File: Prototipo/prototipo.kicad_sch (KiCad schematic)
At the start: 13 parts

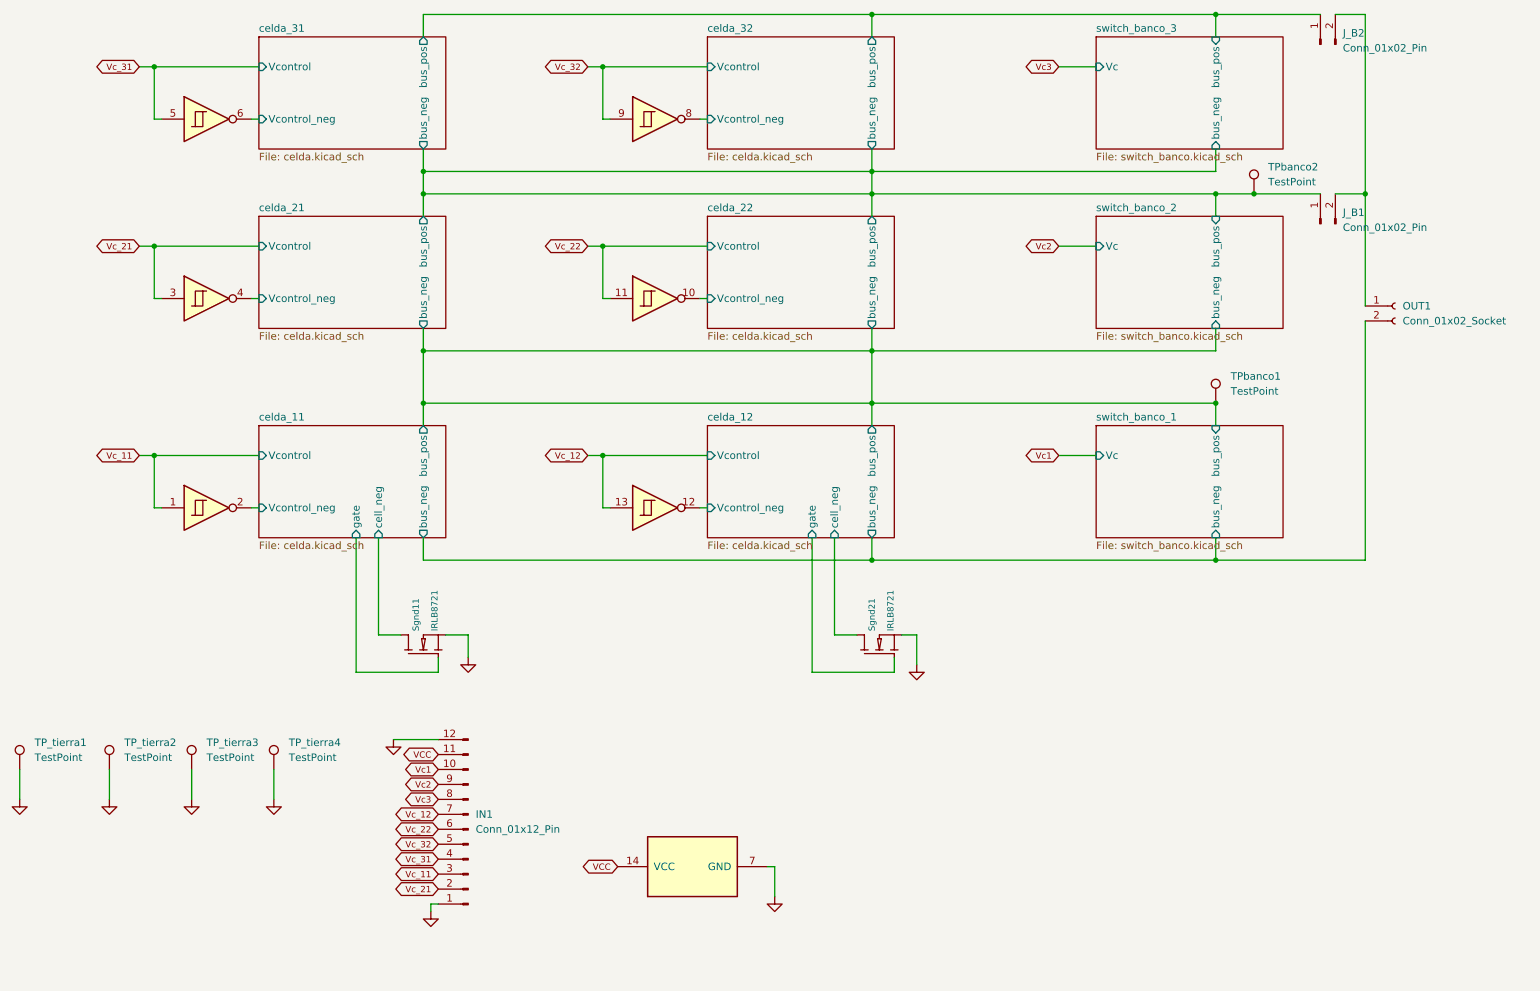
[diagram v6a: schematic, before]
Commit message: doy vuelta el inversor para no tener que hacer tantas vías
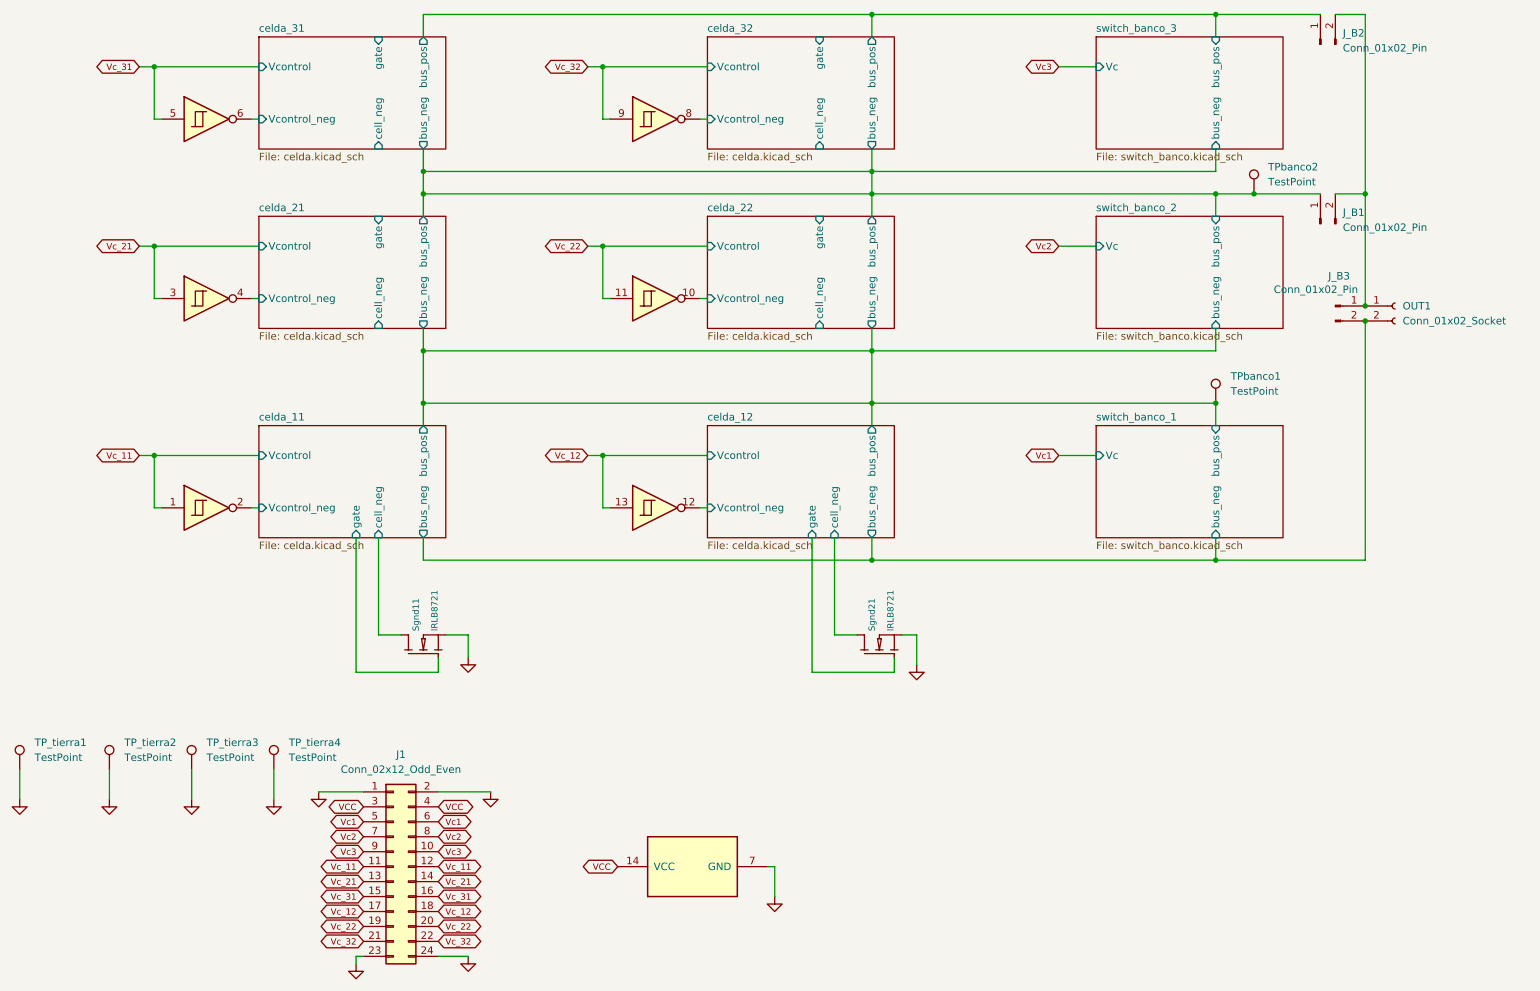
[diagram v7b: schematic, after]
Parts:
- removed IN1: Conn_01x12_Pin, Connector_PinHeader_2.54mm:PinHeader_1x12_P2.54mm_Vertical, symbol Connector:Conn_01x12_Pin
- added J1: Conn_02x12_Odd_Even, Connector_PinHeader_2.54mm:PinHeader_2x12_P2.54mm_Vertical, symbol Connector_Generic:Conn_02x12_Odd_Even
- added J_B3: Conn_01x02_Pin, Connector_PinHeader_2.54mm:PinHeader_1x02_P2.54mm_Vertical, symbol Connector:Conn_01x02_Pin
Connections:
- net 0: now also J1.1 (Pin_1), J1.2 (Pin_2), J1.23 (Pin_23), J1.24 (Pin_24)
- net VCC: now also J1.3 (Pin_3), J1.4 (Pin_4)
- net Vc1: now also J1.5 (Pin_5), J1.6 (Pin_6)
- net Vc2: now also J1.7 (Pin_7), J1.8 (Pin_8)
- net Vc3: now also J1.10 (Pin_10), J1.9 (Pin_9)
- net Vc_11: now also J1.11 (Pin_11), J1.12 (Pin_12)
- net Vc_12: now also J1.17 (Pin_17), J1.18 (Pin_18)
- net Vc_21: now also J1.13 (Pin_13), J1.14 (Pin_14)
- net Vc_22: now also J1.19 (Pin_19), J1.20 (Pin_20)
- net Vc_31: now also J1.15 (Pin_15), J1.16 (Pin_16)
- net Vc_32: now also J1.21 (Pin_21), J1.22 (Pin_22)
- net celda_11/bus_neg: now also J_B3.2 (Pin_2)
- net at J_B1.2 (Pin_2), J_B2.2 (Pin_2), OUT1.1 (Pin_1): now also J_B3.1 (Pin_1)
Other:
- sheet celda_21 ports: added cell_neg, gate; removed none
- sheet celda_22 ports: added cell_neg, gate; removed none
- sheet celda_31 ports: added cell_neg, gate; removed none
- sheet celda_32 ports: added cell_neg, gate; removed none

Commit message: acomodo devuelta el inversor, y agrego conectores para medir con el micro
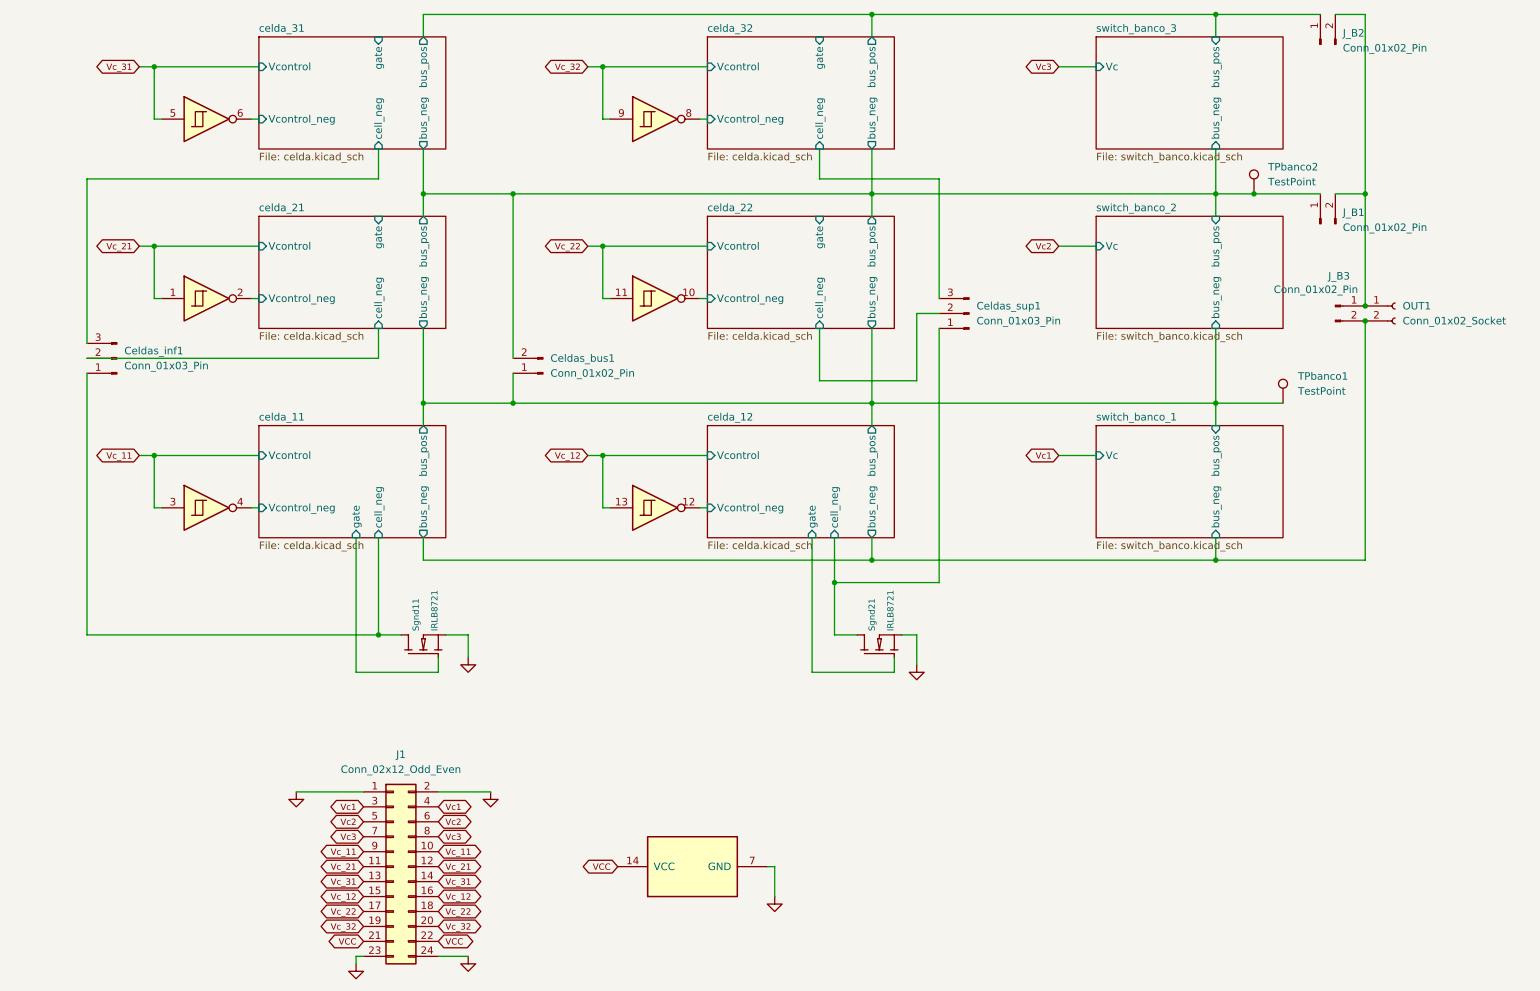
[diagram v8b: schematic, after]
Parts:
- removed TP_tierra1, TP_tierra2, TP_tierra3, TP_tierra4: TestPoint, TestPoint:TestPoint_Bridge_Pitch2.54mm_Drill1.0mm, symbol Connector:TestPoint
- added Celdas_bus1: Conn_01x02_Pin, Connector_PinHeader_2.54mm:PinHeader_1x02_P2.54mm_Vertical, symbol Connector:Conn_01x02_Pin
- added Celdas_inf1, Celdas_sup1: Conn_01x03_Pin, Connector_PinHeader_2.54mm:PinHeader_1x03_P2.54mm_Vertical, symbol Connector:Conn_01x03_Pin
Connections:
- net VCC: now also J1.21 (Pin_21), J1.22 (Pin_22); no longer J1.3 (Pin_3), J1.4 (Pin_4)
- net Vc1: now also J1.3 (Pin_3), J1.4 (Pin_4); no longer J1.5 (Pin_5), J1.6 (Pin_6)
- net Vc2: now also J1.5 (Pin_5), J1.6 (Pin_6); no longer J1.7 (Pin_7), J1.8 (Pin_8)
- net Vc3: now also J1.7 (Pin_7), J1.8 (Pin_8); no longer J1.10 (Pin_10), J1.9 (Pin_9)
- net Vc_11: now also A1.3, J1.10 (Pin_10), J1.9 (Pin_9); no longer A1.1, J1.11 (Pin_11), J1.12 (Pin_12)
- net Vc_12: now also J1.15 (Pin_15), J1.16 (Pin_16); no longer J1.17 (Pin_17), J1.18 (Pin_18)
- net Vc_21: now also A1.1, J1.11 (Pin_11), J1.12 (Pin_12); no longer A1.3, J1.13 (Pin_13), J1.14 (Pin_14)
- net Vc_22: now also J1.17 (Pin_17), J1.18 (Pin_18); no longer J1.19 (Pin_19), J1.20 (Pin_20)
- net Vc_31: now also J1.13 (Pin_13), J1.14 (Pin_14); no longer J1.15 (Pin_15), J1.16 (Pin_16)
- net Vc_32: now also J1.19 (Pin_19), J1.20 (Pin_20); no longer J1.21 (Pin_21), J1.22 (Pin_22)
- net celda_11/Vcontrol_neg: now also A1.4; no longer A1.2
- net celda_11/bus_pos: now also Celdas_bus1.1 (Pin_1)
- net celda_11/cell_neg: now also Celdas_inf1.1 (Pin_1)
- net celda_12/cell_neg: now also Celdas_sup1.1 (Pin_1)
- net celda_21/Vcontrol_neg: now also A1.2; no longer A1.4
- net celda_21/bus_pos: now also Celdas_bus1.2 (Pin_2)
- net celda_21/cell_neg: now also Celdas_inf1.2 (Pin_2)
- net celda_22/cell_neg: now also Celdas_sup1.2 (Pin_2)
- net celda_31/cell_neg: now also Celdas_inf1.3 (Pin_3)
- net celda_32/cell_neg: now also Celdas_sup1.3 (Pin_3)
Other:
- moved on the sheet: TPbanco1
